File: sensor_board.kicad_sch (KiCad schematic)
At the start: 50 parts, among them J5 TagConnect_TC2030_SWD, U1 AMS1117-3.3, U15 CJ431, U16 7408, U2 STM32H753IITx

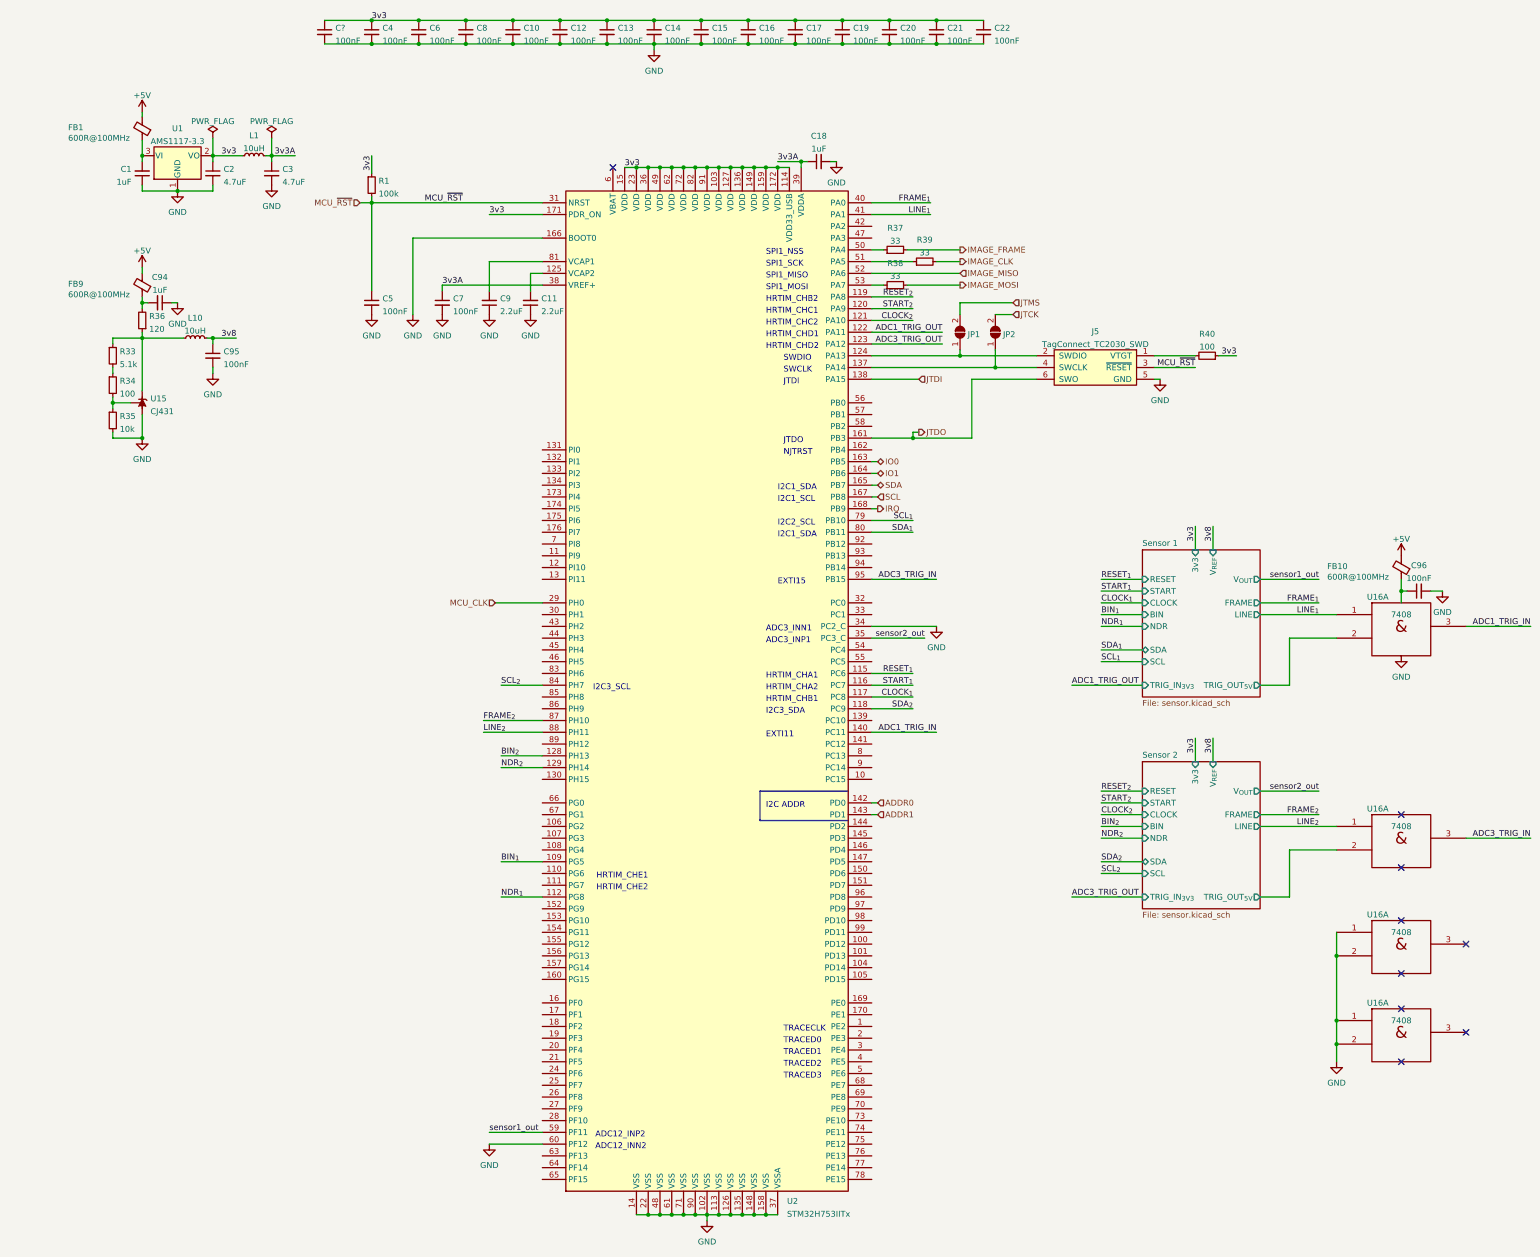
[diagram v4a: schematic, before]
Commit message: Decouple MCU resets via diode
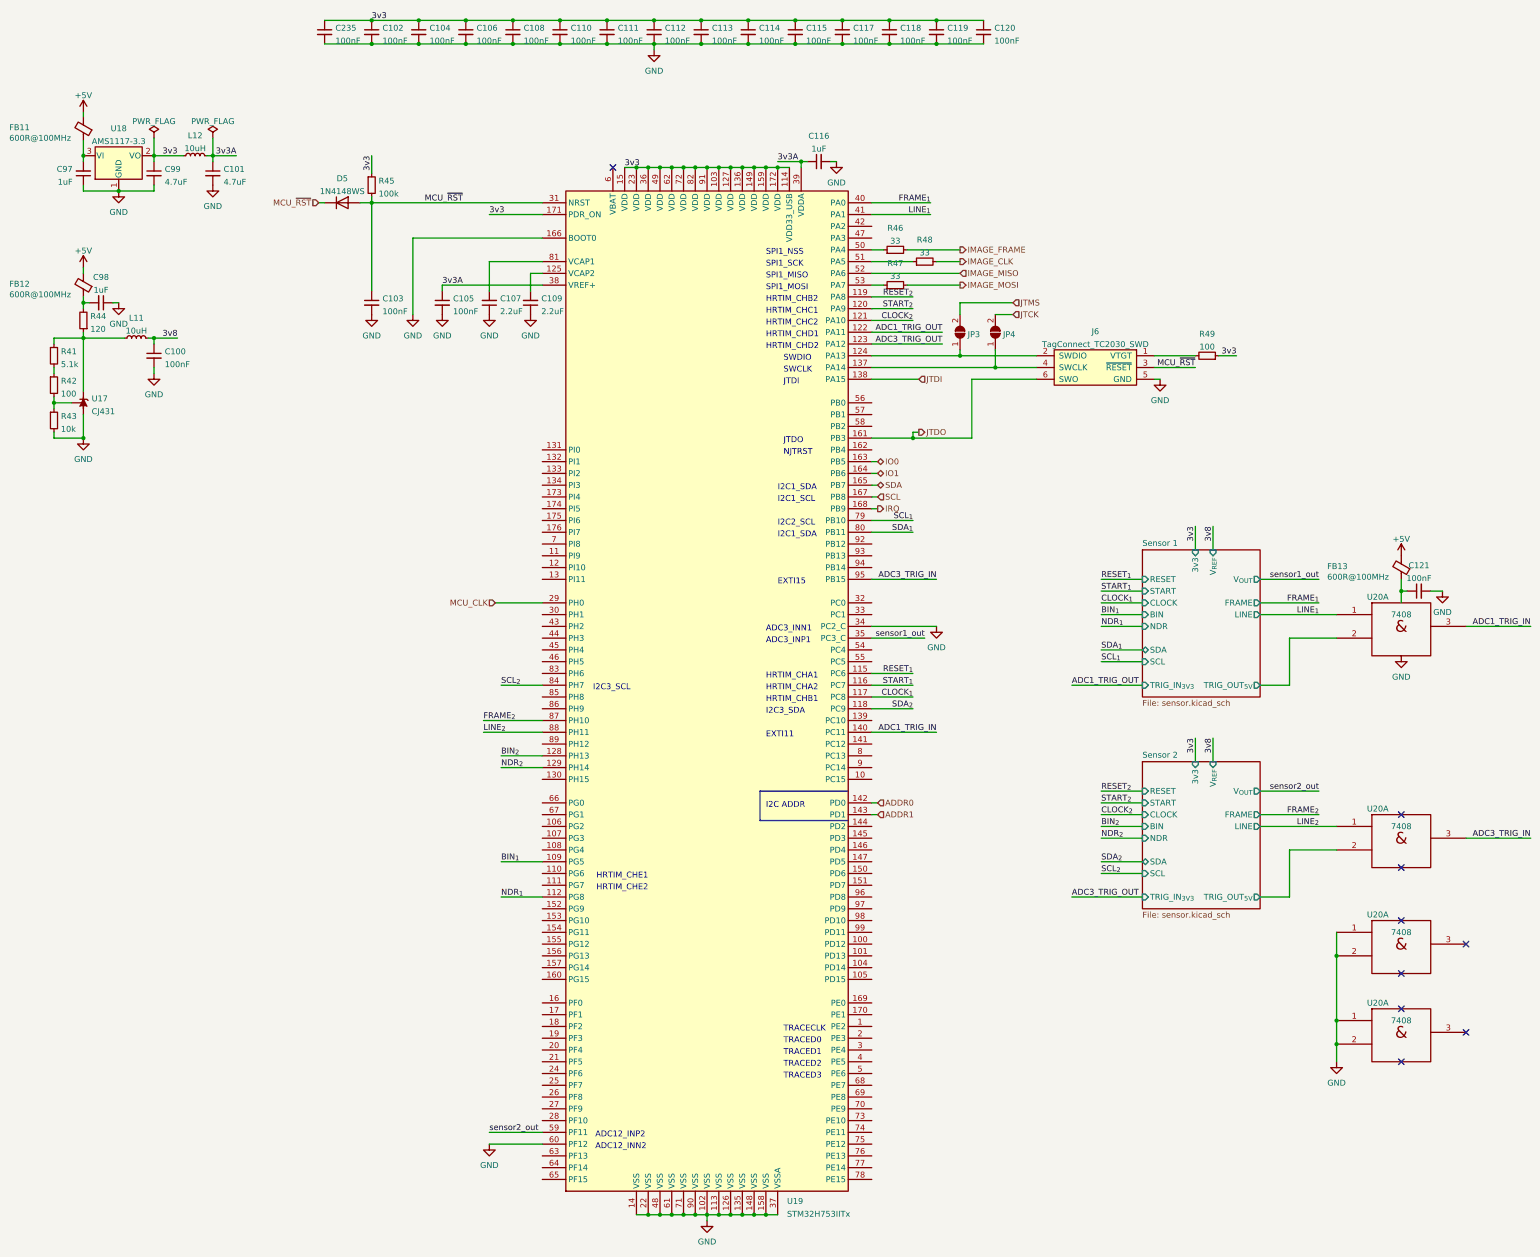
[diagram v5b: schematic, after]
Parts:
- added D5: 1N4148WS, Diode_SMD:D_SOD-323, symbol Device:D
- gave numbers to parts that had none: 1
- renumbered C95 to C100, C3 to C101, C4 to C102, C5 to C103, C6 to C104, C7 to C105, C8 to C106, C9 to C107, C10 to C108, C11 to C109, C12 to C110, C13 to C111, C14 to C112, C15 to C113, C16 to C114, C17 to C115, C18 to C116, C19 to C117, C20 to C118, C21 to C119, C22 to C120, C96 to C121, C1 to C97, C94 to C98, C2 to C99, FB1 to FB11, FB9 to FB12, FB10 to FB13, J5 to J6, JP1 to JP3, JP2 to JP4, L10 to L11, L1 to L12, R33 to R41, R34 to R42, R35 to R43, R36 to R44, R1 to R45, R37 to R46, R38 to R47, R39 to R48, R40 to R49, U15 to U17, U1 to U18, U2 to U19, U16 to U20
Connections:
- net MCU_~{RST}: now also D5.1 (K), D5.2 (A)
- net sensor1_out: now also U19.35 (PC3_C); no longer U19.59 (PF11)
- net sensor2_out: now also U19.59 (PF11); no longer U19.35 (PC3_C)
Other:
- moved on the sheet: C100, C101, C97, C98, C99, FB11, FB12, L11, L12, R41, R42, R43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

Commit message: Use two instead of four 3.8V voltage references
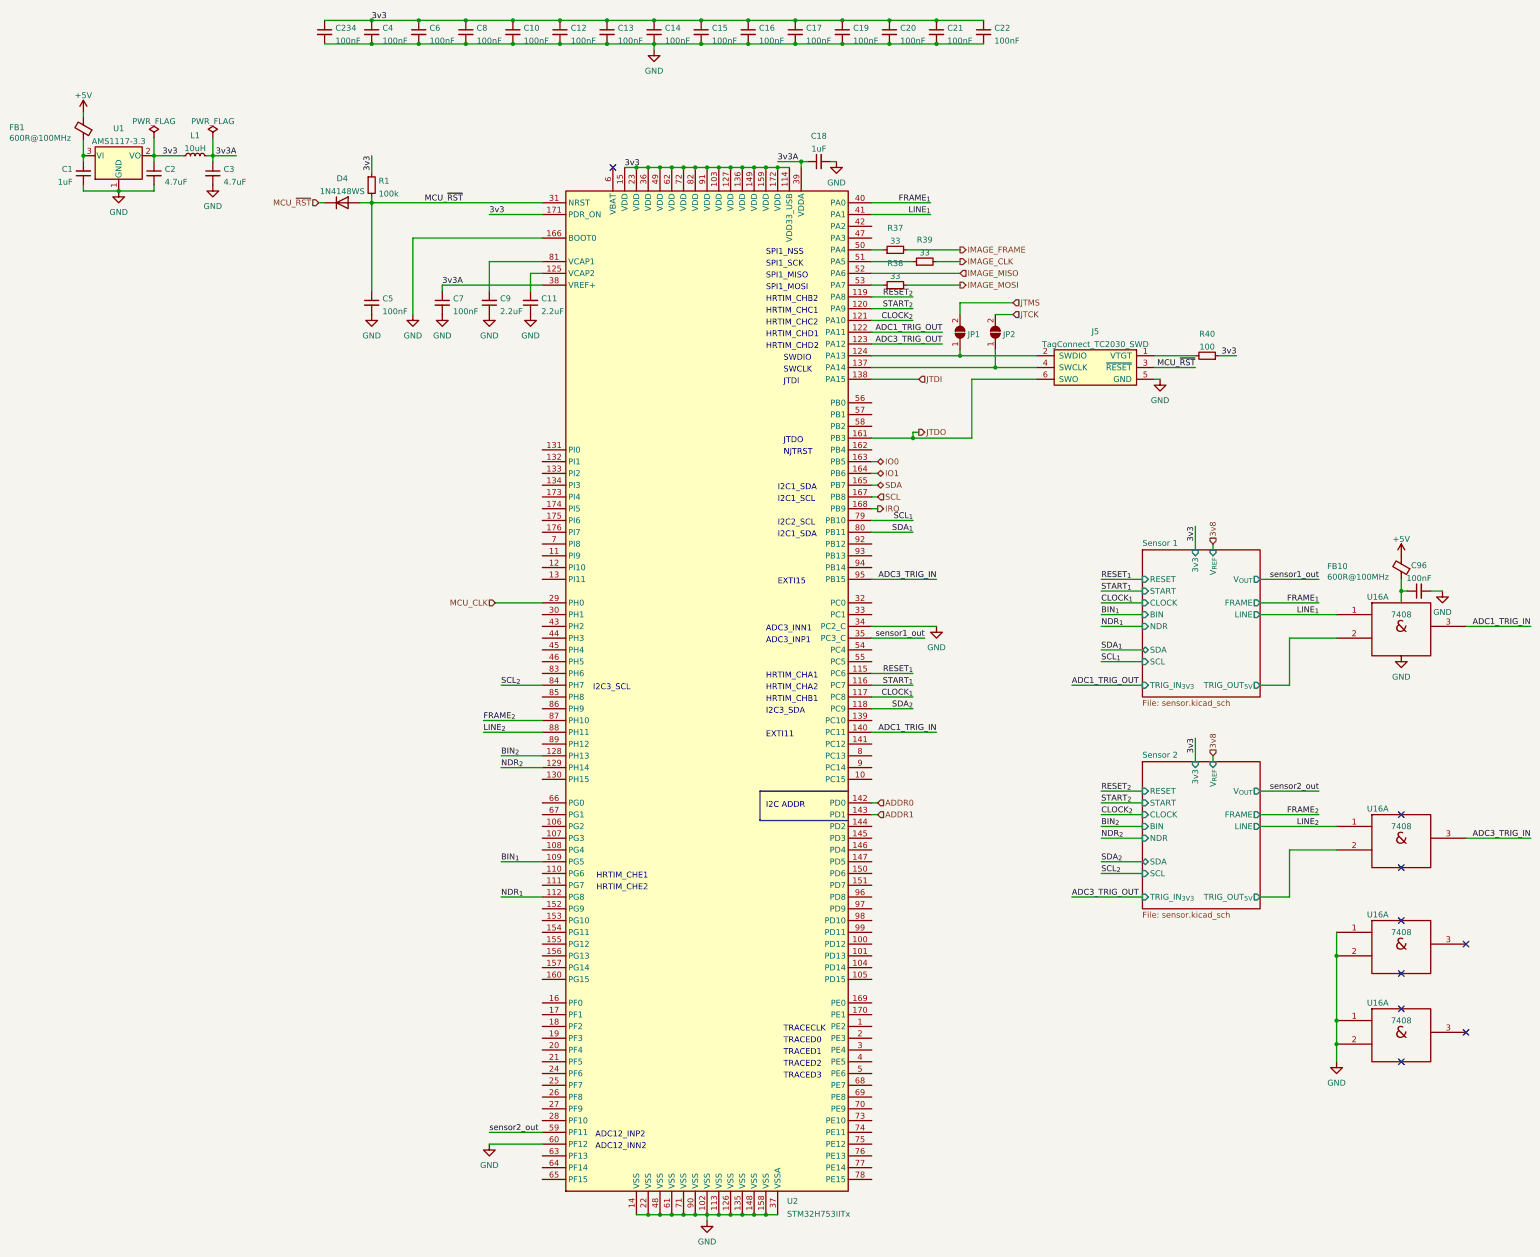
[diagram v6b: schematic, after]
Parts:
- removed C100: 100nF, Capacitor_SMD:C_0402_1005Metric, symbol Device:C_Small
- removed C98: 1uF, Capacitor_SMD:C_0402_1005Metric, symbol Device:C_Small
- removed FB12: 600R@100MHz, Inductor_SMD:L_0805_2012Metric, symbol Device:FerriteBead_Small
- removed L11: 10uH, Inductor_SMD:L_0805_2012Metric, symbol Device:L_Small
- removed R41: 5.1k, Resistor_SMD:R_0402_1005Metric, symbol Device:R_Small
- removed R42: 100, Resistor_SMD:R_0402_1005Metric, symbol Device:R_Small
- removed R43: 10k, Resistor_SMD:R_0402_1005Metric, symbol Device:R_Small
- removed R44: 120, Resistor_SMD:R_0805_2012Metric, symbol Device:R_Small
- removed U17: CJ431, Package_TO_SOT_SMD:SOT-23, symbol Reference_Voltage:TL431DBZ
- renumbered C97 to C1, C108 to C10, C109 to C11, C110 to C12, C111 to C13, C112 to C14, C113 to C15, C114 to C16, C115 to C17, C116 to C18, C117 to C19, C99 to C2, C118 to C20, C119 to C21, C120 to C22, C235 to C234, C101 to C3, C102 to C4, C103 to C5, C104 to C6, C105 to C7, C106 to C8, C107 to C9, C121 to C96, D5 to D4, FB11 to FB1, FB13 to FB10, J6 to J5, JP3 to JP1, JP4 to JP2, L12 to L1, R45 to R1, R46 to R37, R47 to R38, R48 to R39, R49 to R40, U18 to U1, U20 to U16, U19 to U2

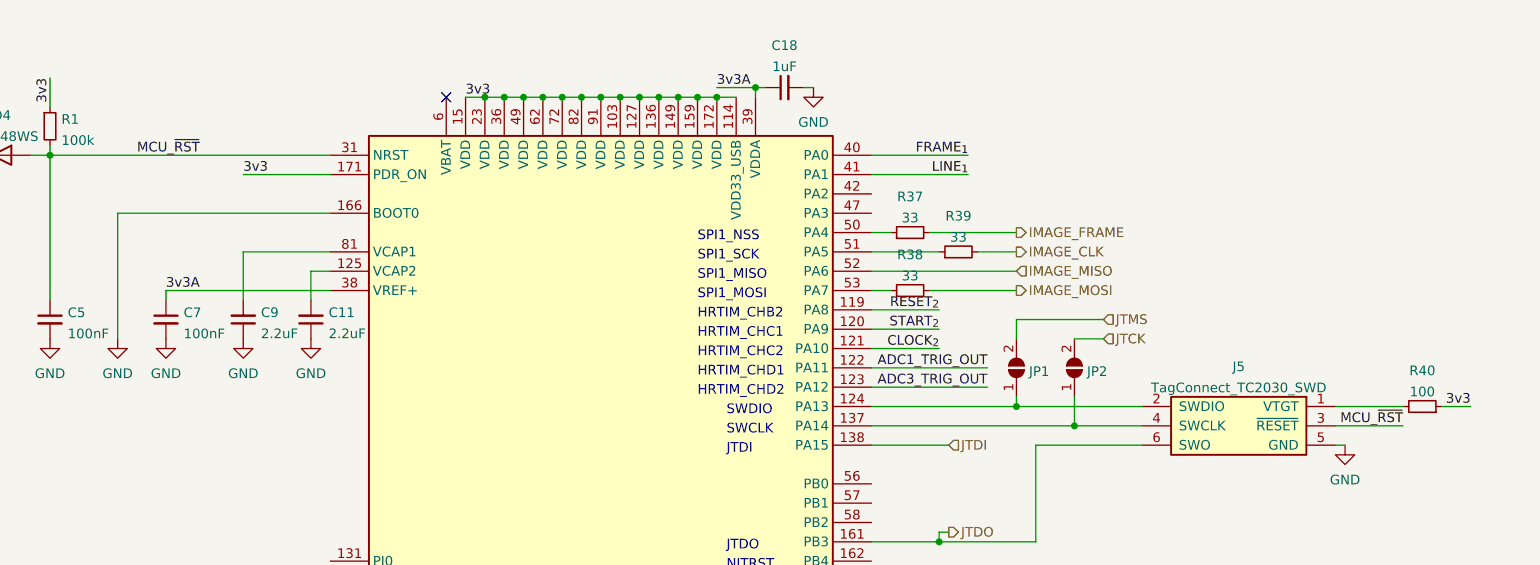
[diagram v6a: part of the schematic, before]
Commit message: Fix broken SPI net labels
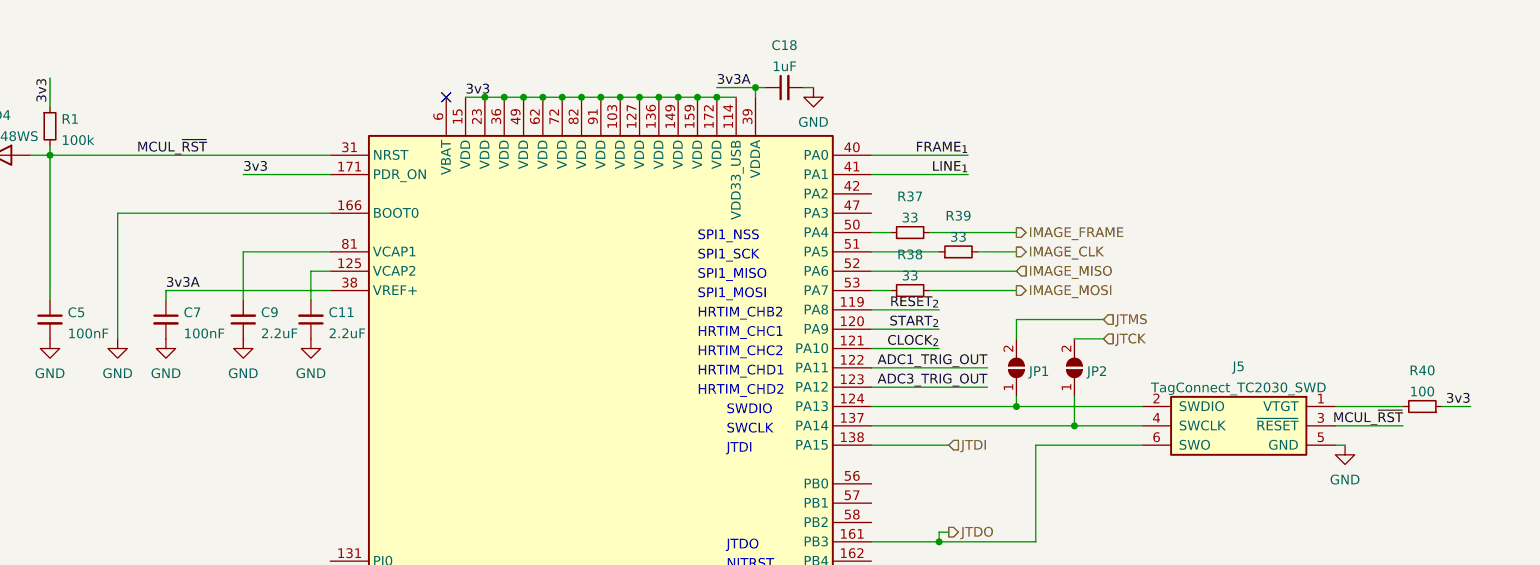
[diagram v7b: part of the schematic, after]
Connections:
- net MCU_~{RST}: no longer C5.1, D4.2 (A), J5.3 (~{RESET}), R1.2, U2.31 (NRST)
- new net MCUL_~{RST}: C5.1, D4.2 (A), J5.3 (~{RESET}), R1.2, U2.31 (NRST)
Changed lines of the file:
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@@
     (effects (font (size 1.27 1.27)) (justify left bottom))
   )
-  (label "MCU_~{RST}" (at 289.56 93.98 180)
+  (label "MCUL_~{RST}" (at 289.56 93.98 180)
     (effects (font (size 1.27 1.27)) (justify right bottom))
   )
@@
     (effects (font (size 1.27 1.27)) (justify right bottom))
   )
-  (label "MCU_~{RST}" (at 123.19 58.42 0)
+  (label "MCUL_~{RST}" (at 123.19 58.42 0)
     (effects (font (size 1.27 1.27)) (justify left bottom))
   )
